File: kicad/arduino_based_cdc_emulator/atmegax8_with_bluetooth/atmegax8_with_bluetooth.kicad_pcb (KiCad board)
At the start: 2 copper layers, 67 parts, among them IC1 ATMEGA88-A, P1 CONN_9, P2 SPI, Q1 BC817-40, U1 78L05, U2 S3860M-S, U3 LM358, X1 16MHz

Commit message: PCB layout work
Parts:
- C10, P1: moved to B.Cu
- C17, C18, R22, R24: moved to F.Cu
- moved C24 96.1 mm to (133.3, 188.2)
- moved R7 84.9 mm to (136.3, 182.6)
- moved D1 71.9 mm to (125.6, 186.8)
- moved C11 68.1 mm to (87.9, 195.4)
- moved L1 62.4 mm to (93.7, 181.5)
- moved C13 56.4 mm to (88.8, 191.0)
- moved R17 55.6 mm to (90.2, 186.4), turned to 90 degrees
- moved C10 51.5 mm to (100.2, 169.7)
- moved R16 49.3 mm to (90.2, 181.3), turned to 90 degrees
- moved C12 46.7 mm to (87.6, 183.2), turned to 270 degrees
- moved R25 40.8 mm to (124.8, 161.3)
- moved C25 37.6 mm to (125.1, 155.4)
- moved R28 37.6 mm to (123.6, 165.3)
- moved C24 37.6 mm to (125.2, 158.3)
- moved Q1 37.6 mm to (128.1, 168.3)
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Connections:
- C23 pad 2: /MIC -> /MIC_IN
- P1 pad 2: /AOUTR -> GNDA
- P1 pad 3: GNDA -> /AOUTR
- P1 pad 4: /MIC -> /MIC_IN
- R27 pad 1: /MIC -> /MIC_IN
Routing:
- net GNDA: track 7.07 -> 66.4 mm, vias 0 -> 1
- net /MIC: track 0.00 -> 27.5 mm
- net +12C: track 0.55 -> 26.9 mm, vias 0 -> 1
- net /MIC_BIAS: track 0.48 -> 24.7 mm
- net Net-(C17-Pad1): track 4.86 -> 24.3 mm, vias 0 -> 1
- net +12V: track 6.86 -> 25.9 mm
- net /VGND: track 6.96 -> 22.0 mm
- net /AOUTL: track 25.6 -> 39.7 mm, vias 1 -> 0
- net GND: track 26.6 -> 38.0 mm
- net Net-(C15-Pad2): track 24.9 -> 13.8 mm
- net /AOUTR: track 2.83 -> 12.5 mm
- net Net-(C14-Pad1): track 16.0 -> 9.36 mm
- net /MIC_IN: track 0.00 -> 6.42 mm
- net Net-(C15-Pad1): track 19.1 -> 13.5 mm
- net Net-(C20-Pad2): track 6.34 -> 3.19 mm
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
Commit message: PCB layout work
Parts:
- removed the C24 at (133.3, 188.2)
- C24: value 2u1 -> 2u2; moved to B.Cu
- C5, P2: moved to B.Cu
- moved R7 30.4 mm to (108.5, 170.1)
- moved D1 22.3 mm to (108.4, 172.6), turned to 0 degrees
- moved R25 21.0 mm to (116.3, 180.5)
- moved Q1 21.0 mm to (107.6, 172.9), turned to 180 degrees
- moved R4 16.7 mm to (111.7, 174.0), turned to 180 degrees
- moved R19 16.7 mm to (116.3, 186.8)
- moved C25 16.2 mm to (113.9, 167.1), turned to 90 degrees
- moved C5 15.6 mm to (108.4, 168.2), turned to 0 degrees
- moved R13 14.6 mm to (111.6, 177.9)
- moved C24 14.4 mm to (113.8, 167.2), turned to 90 degrees
- moved R28 13.4 mm to (110.4, 167.3), turned to 90 degrees
- moved C1 8.87 mm to (107.9, 196.7)
- moved C2 8.20 mm to (97.5, 196.7)
- moved R6 7.77 mm to (102.7, 196.7), turned to 180 degrees
- moved R5 6.83 mm to (98.9, 189.3), turned to 0 degrees
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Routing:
- net GND: track 38.0 -> 96.1 mm
- net /ARESET: track 0.00 -> 25.8 mm
- net Net-(C1-Pad1): track 0.00 -> 24.3 mm
- net RX: track 0.00 -> 22.1 mm, vias 0 -> 1
- net /BT_RESET: track 0.00 -> 19.9 mm
- net +5V: track 0.00 -> 19.8 mm
- net Net-(R25-Pad1): track 0.00 -> 19.7 mm, vias 0 -> 1
- net TX: track 0.00 -> 18.9 mm, vias 0 -> 1
- net +BATT: track 0.00 -> 12.0 mm
- net /CDC_ENA_5V: track 0.00 -> 11.0 mm
- net Net-(C2-Pad1): track 0.00 -> 10.5 mm
- net /DataIn: track 0.00 -> 10.2 mm
- net Net-(IC1-Pad31): track 0.00 -> 8.36 mm
- net /Clock: track 0.00 -> 7.75 mm
- net Net-(P1-Pad9): track 0.00 -> 7.58 mm
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
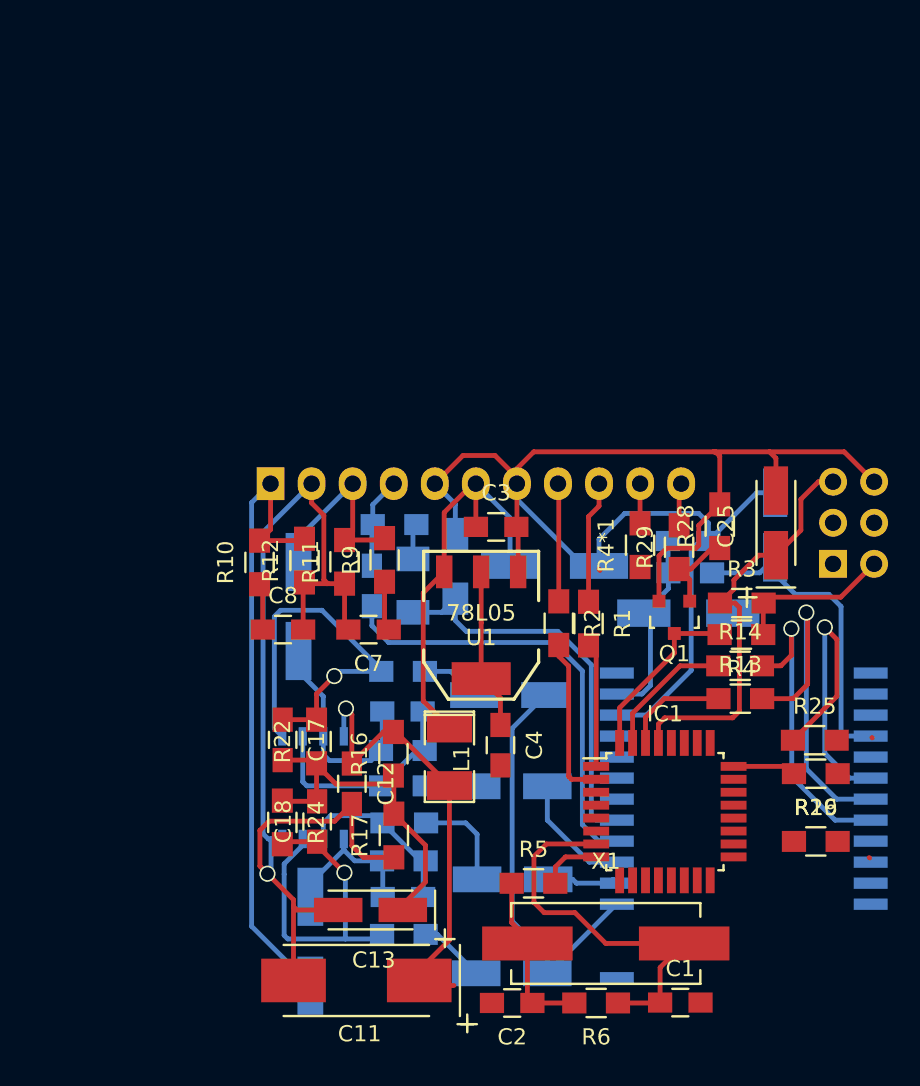
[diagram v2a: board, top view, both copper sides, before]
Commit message: finished? I gues yes, board for vwcdavr emulator with bluetooth
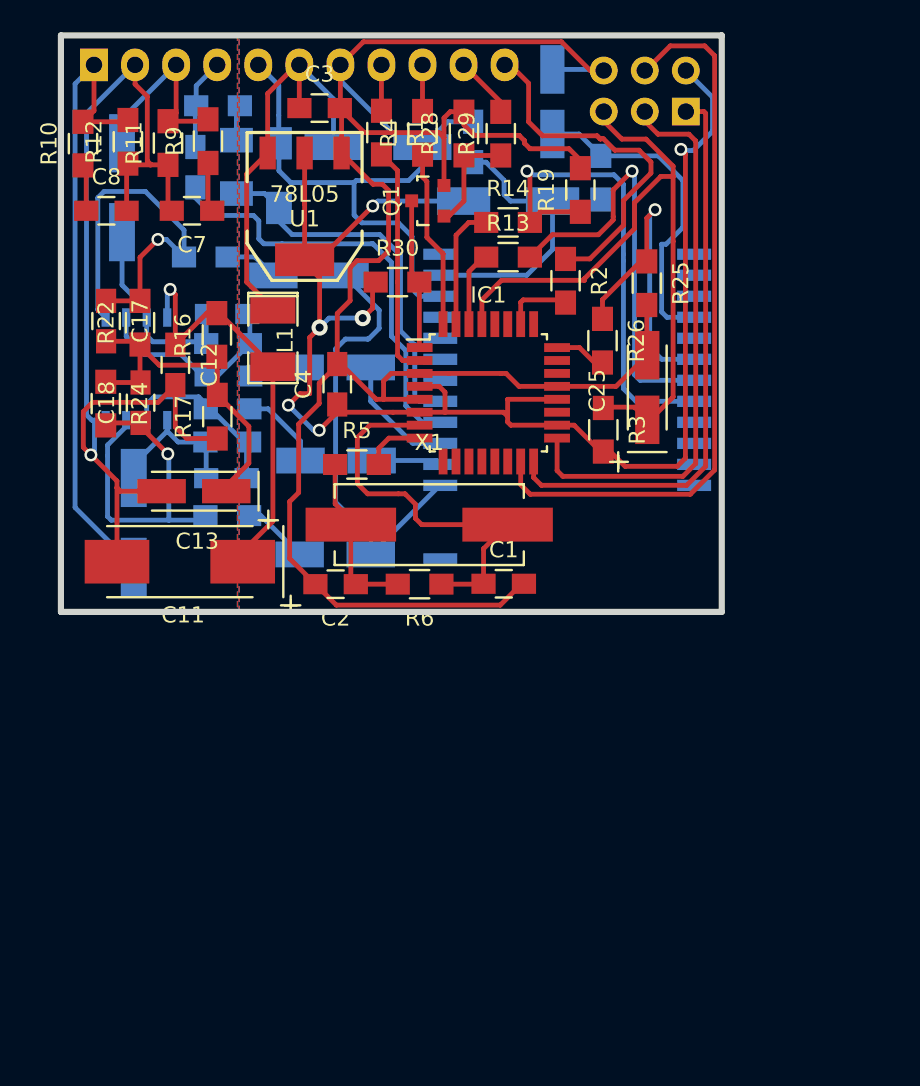
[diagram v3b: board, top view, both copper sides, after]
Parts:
- moved R19 42.8 mm to (101.8, 146.5), turned to 90 degrees
- moved R1 33.0 mm to (89.4, 142.9)
- moved R14 31.0 mm to (97.3, 148.5)
- moved R13 30.9 mm to (97.3, 150.6)
- moved R30 30.5 mm to (90.4, 152.2), turned to 0 degrees
- moved R25 30.1 mm to (105.9, 152.2), turned to 270 degrees
- moved Q1 29.9 mm to (92.3, 147.1), turned to 90 degrees
- moved R26 29.9 mm to (103.1, 155.8), turned to 270 degrees
- moved C24 29.6 mm to (100.0, 141.0)
- moved P2 29.4 mm to (108.3, 141.6), turned to 90 degrees
- moved R28 29.0 mm to (94.6, 143.0)
- moved R4 28.8 mm to (92.0, 142.9)
- moved C19 28.8 mm to (85.0, 151.7)
- moved R20 28.4 mm to (78.6, 150.6)
- moved C11 28.1 mm to (77.0, 169.4)
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- renumbered R4 to R30, R4*1 to R4
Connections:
- IC1 pad 1: /Clock -> /CDC_ENA_5V
- IC1 pad 12: Net-(IC1-Pad12) -> (no net)
- IC1 pad 2: /DataIn -> /Clock
- IC1 pad 26: (no net) -> /DataIn
- IC1 pad 32: /CDC_ENA_5V -> Net-(IC1-Pad32)
- P1 pad 10: /DataOut -> /CDC_ENA_12V
- P1 pad 11: /CDC_ENA_12V -> Net-(P1-Pad11)
- P1 pad 9: Net-(P1-Pad9) -> /DataOut
- R1 pad 1: Net-(P1-Pad9) -> Net-(P1-Pad8)
- R2 pad 1: Net-(P1-Pad8) -> Net-(P1-Pad11)
- R4 pad 1: Net-(IC1-Pad12) -> Net-(IC1-Pad32)
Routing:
- net +5V: track 19.8 -> 95.4 mm, vias 0 -> 6
- net GND: track 96.1 -> 169.3 mm
- net /MOSI: track 0.00 -> 45.1 mm
- net /SCK: track 0.00 -> 35.9 mm
- net /MISO: track 0.00 -> 35.4 mm
- net Net-(P1-Pad11): track 0.00 -> 22.6 mm
- net /ARESET: track 25.8 -> 43.5 mm
- net TX: track 18.9 -> 30.7 mm
- net Net-(IC1-Pad32): track 0.00 -> 11.0 mm
- net +BATT: track 12.0 -> 20.7 mm
- net Net-(P1-Pad9): track 7.58 -> 0.00 mm
- net /Clock: track 7.75 -> 14.3 mm
- net /DataIn: track 10.2 -> 4.30 mm
- net Net-(P1-Pad8): track 7.30 -> 2.91 mm
- net RX: track 22.1 -> 26.1 mm
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- added copper zone on B.Cu, net GND
- added copper zone on F.Cu, net GND
- added copper zone on B.Cu, net GNDA
- added copper zone on F.Cu, net GNDA
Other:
- board outline added: 40.9 x 35.7 mm
- net class Default: clearance 0.254 -> 0.2; via_dia 1 -> 0.8; via_drill 0.8 -> 0.5
- rule trace_clearance: 0.254 -> 0.2
- rule via_min_drill: 0.508 -> 0.5
- rule via_min_size: 0.889 -> 0.5

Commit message: updates, I do not remember what I changed ....
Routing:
- net +5V: track 95.4 -> 94.3 mm
- net /BTAGND: track 27.1 -> 26.5 mm

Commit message: updates
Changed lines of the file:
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@@
-(kicad_pcb (version 4) (host pcbnew 0.201603091917+6614~43~ubuntu14.04.1-product)
+(kicad_pcb (version 20170123) (host pcbnew no-vcs-found-7602~57~ubuntu16.04.1)
   (general
     (links 130)
@@
     (pad 2 smd rect (at 4.84886 0) (size 5.6007 2.10058) (layers Front F.Paste F.Mask)
       (net 9 "Net-(C1-Pad1)"))
+    (model /home/nail/src/kicad/modules/packages3d/Crystals_Oscillators_SMD.3dshapes/Q_49U3HMS.wrl
+      (at (xyz 0 0 0))
+      (scale (xyz 1 1 1))
+      (rotate (xyz 0 0 0))
+    )
   )
   (module my_modules:S3860M-S (layer Back)
@@
     (pad GND smd rect (at -2.286 3.302 180) (size 1.016 2.032) (layers Front F.Paste F.Mask)
       (net 3 GND))
-    (model smd/SOT223.wrl
+    (model /home/nail/src/kicad/KiCad/3d_models/ab2_sot/AB2_SOT223.wrl
       (at (xyz 0 0 0))
       (scale (xyz 0.4 0.4 0.4))
@@
     (tags "capacitor 0805")
     (attr smd)
-    (fp_text reference C3 (at 0 -2.1) (layer F.SilkS)
+    (fp_text reference C3 (at -2.8194 -0.0381 90) (layer F.SilkS)
       (effects (font (size 1 1) (thickness 0.15)))
     )
@@
     (tags "resistor 0805")
     (attr smd)
-    (fp_text reference R1 (at 2.91592 0.72644 360) (layer F.SilkS)
+    (fp_text reference R1 (at 2.91592 0.72644) (layer F.SilkS)
       (effects (font (size 1 1) (thickness 0.15)))
     )
@@
     (tags "resistor 0805")
     (attr smd)
-    (fp_text reference R4 (at -3.00228 -1.26492 360) (layer F.SilkS)
+    (fp_text reference R4 (at -3.00228 -1.26492) (layer F.SilkS)
       (effects (font (size 1 1) (thickness 0.15)))
     )
@@
     (tags "resistor 0805")
     (attr smd)
-    (fp_text reference R3 (at 3.1496 0.127 540) (layer F.SilkS)
+    (fp_text reference R3 (at 3.1496 0.127 180) (layer F.SilkS)
       (effects (font (size 1 1) (thickness 0.15)))
     )
@@
     (tags "resistor 0805")
     (attr smd)
-    (fp_text reference R18 (at 2.74828 -0.86868 450) (layer B.SilkS)
+    (fp_text reference R18 (at 2.74828 -0.86868 90) (layer B.SilkS)
       (effects (font (size 1 1) (thickness 0.15)) (justify mirror))
     )
@@
     (tags "resistor 0805")
     (attr smd)
-    (fp_text reference R25 (at -3.0734 0.0762 540) (layer F.SilkS)
+    (fp_text reference R25 (at -3.0734 0.0762 180) (layer F.SilkS)
       (effects (font (size 1 1) (thickness 0.15)))
     )
@@
     (tags "resistor 0805")
     (attr smd)
-    (fp_text reference R26 (at -3.7338 -0.508 450) (layer F.SilkS)
-      (effects (font (size 1 1) (thickness 0.15)))
-    )
+    (fp_text reference R26 (at -3.7338 -0.508 90) (layer F.SilkS)
+      (effects (font (size 1 1) (thickness 0.15)))
+    )
